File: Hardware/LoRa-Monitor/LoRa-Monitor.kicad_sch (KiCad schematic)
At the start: 0 parts

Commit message: Deleted lck files
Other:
- sheet Energy Meter Interface Module ports: added 485_A, 485_B, EN_485, PULSE_IN1+, PULSE_IN1-, PULSE_IN1_3V3, PULSE_IN2+, PULSE_IN2-, PULSE_IN2_3V3, PULSE_IN3+, PULSE_IN3-, PULSE_IN3_3V3, RXD_485, TXD_485; removed none
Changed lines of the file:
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@@
 	(paper "A4")
 	(sheet
-		(at 59.69 109.22)
+		(at 69.215 40.64)
 		(size 35.56 16.51)
 		(exclude_from_sim no)
@@
 		)
 		(property "Sheetname" "MCU"
-			(at 59.69 108.5084 0)
+			(at 69.215 39.9284 0)
 			(show_name no)
 			(do_not_autoplace no)
@@
 		)
 		(property "Sheetfile" "MCU.kicad_sch"
-			(at 59.69 126.3146 0)
+			(at 69.215 57.7346 0)
 			(show_name no)
 			(do_not_autoplace no)
@@
 	)
 	(sheet
-		(at 137.16 104.775)
+		(at 31.75 20.955)
 		(size 57.785 17.145)
 		(exclude_from_sim no)
@@
 		)
 		(property "Sheetname" "Power supply"
-			(at 137.16 104.0634 0)
+			(at 31.75 20.2434 0)
 			(show_name no)
 			(do_not_autoplace no)
@@
 		)
 		(property "Sheetfile" "PowerSupply.kicad_sch"
-			(at 137.16 122.5046 0)
+			(at 31.75 38.6846 0)
 			(show_name no)
 			(do_not_autoplace no)
@@
 			)
 		)
+		(pin "PULSE_IN2+" input
+			(at 48.26 69.85 90)
+			(effects
+				(font
+					(size 1.27 1.27)
+				)
+				(justify right)
+			)
+		)
+		(pin "PULSE_IN2-" input
+			(at 49.8793 69.85 90)
+			(effects
+				(font
+					(size 1.27 1.27)
+				)
+				(justify right)
+			)
+		)
+		(pin "PULSE_IN3+" input
+			(at 51.4986 69.85 90)
+			(effects
+				(font
+					(size 1.27 1.27)
+				)
+				(justify right)
+			)
+		)
+		(pin "PULSE_IN3-" input
+			(at 53.1179 69.85 90)
+			(effects
+				(font
+					(size 1.27 1.27)
+				)
+				(justify right)
+			)
+		)
+		(pin "RXD_485" output
+			(at 54.7372 69.85 90)
+			(effects
+				(font
+					(size 1.27 1.27)
+				)
+				(justify right)
+			)
+		)
+		(pin "EN_485" input
+			(at 56.3565 69.85 90)
+			(effects
+				(font
+					(size 1.27 1.27)
+				)
+				(justify right)
+			)
+		)
+		(pin "PULSE_IN1_3V3" output
+			(at 57.9758 69.85 90)
+			(effects
+				(font
+					(size 1.27 1.27)
+				)
+				(justify right)
+			)
+		)
+		(pin "PULSE_IN3_3V3" output
+			(at 59.5951 69.85 90)
+			(effects
+				(font
+					(size 1.27 1.27)
+				)
+				(justify right)
+			)
+		)
+		(pin "PULSE_IN2_3V3" output
+			(at 61.2144 69.85 90)
+			(effects
+				(font
+					(size 1.27 1.27)
+				)
+				(justify right)
+			)
+		)
+		(pin "TXD_485" input
+			(at 62.8337 69.85 90)
+			(effects
+				(font
+					(size 1.27 1.27)
+				)
+				(justify right)
+			)
+		)
+		(pin "485_A" bidirectional
+			(at 64.453 69.85 90)
+			(effects
+				(font
+					(size 1.27 1.27)
+				)
+				(justify right)
+			)
+		)
+		(pin "485_B" bidirectional
+			(at 80.01 85.09 0)
+			(effects
+				(font
+					(size 1.27 1.27)
+				)
+				(justify right)
+			)
+		)
+		(pin "PULSE_IN1+" input
+			(at 48.26 77.5578 180)
+			(effects
+				(font
+					(size 1.27 1.27)
+				)
+				(justify left)
+			)
+		)
+		(pin "PULSE_IN1-" input
+			(at 61.7736 69.85 90)
+			(effects
+				(font
+					(size 1.27 1.27)
+				)
+				(justify right)
+			)
+		)

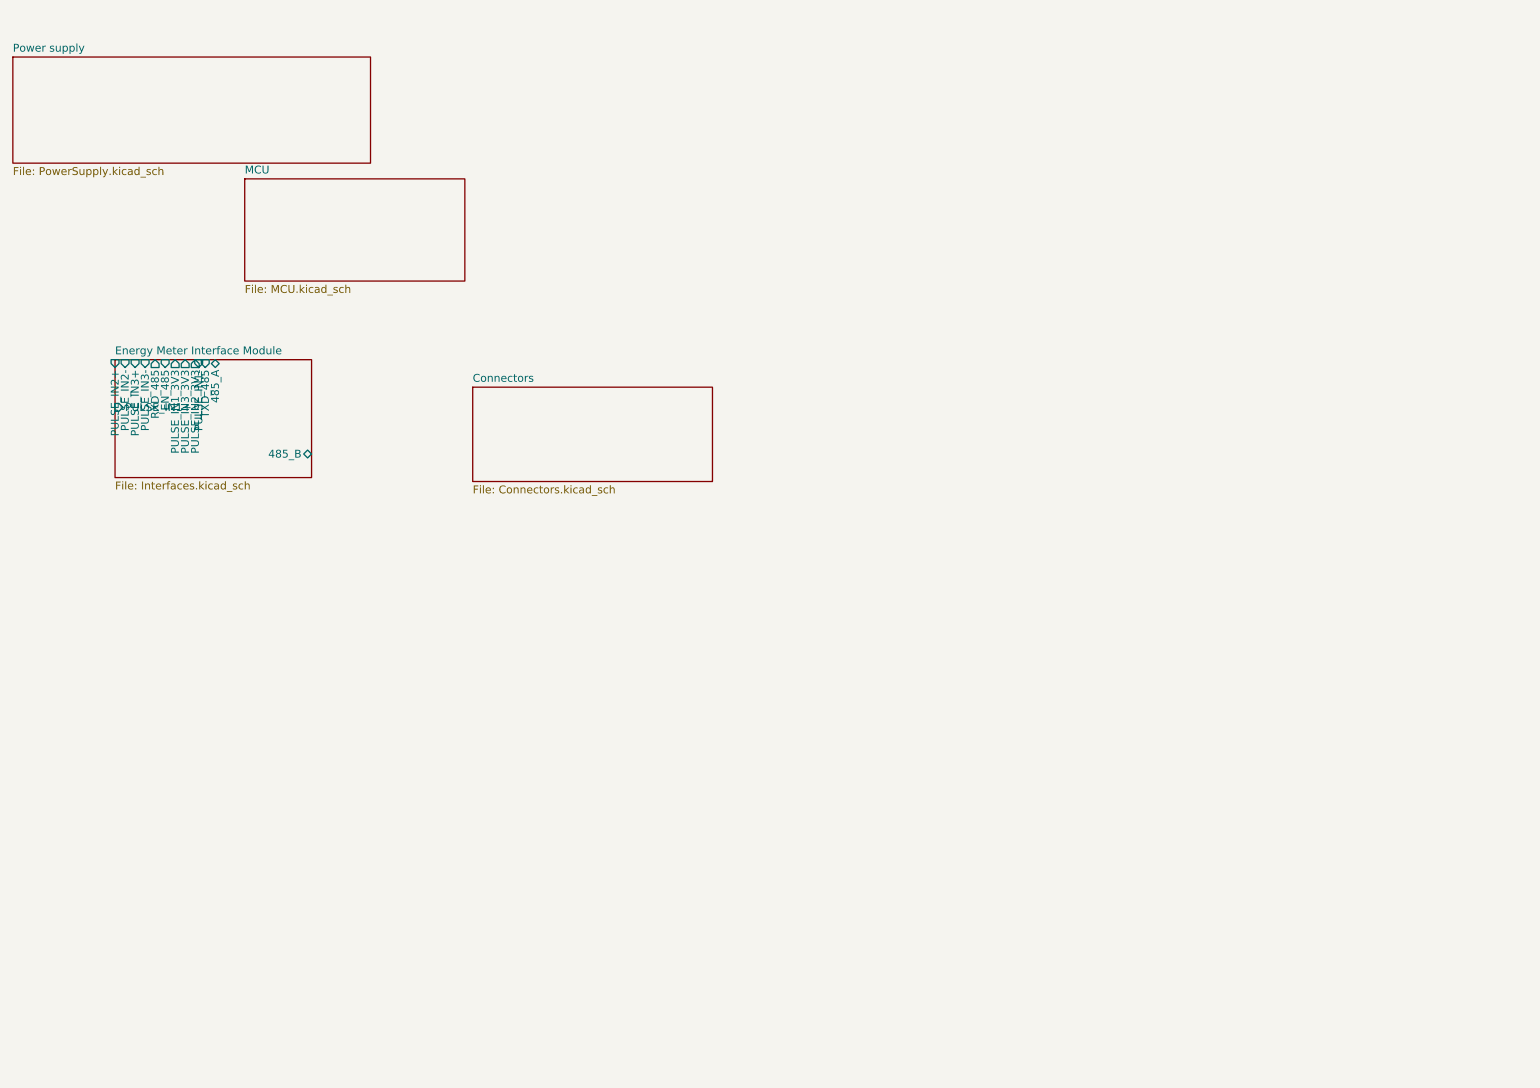
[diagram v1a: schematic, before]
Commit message: Finished PSU module, started Energy meter
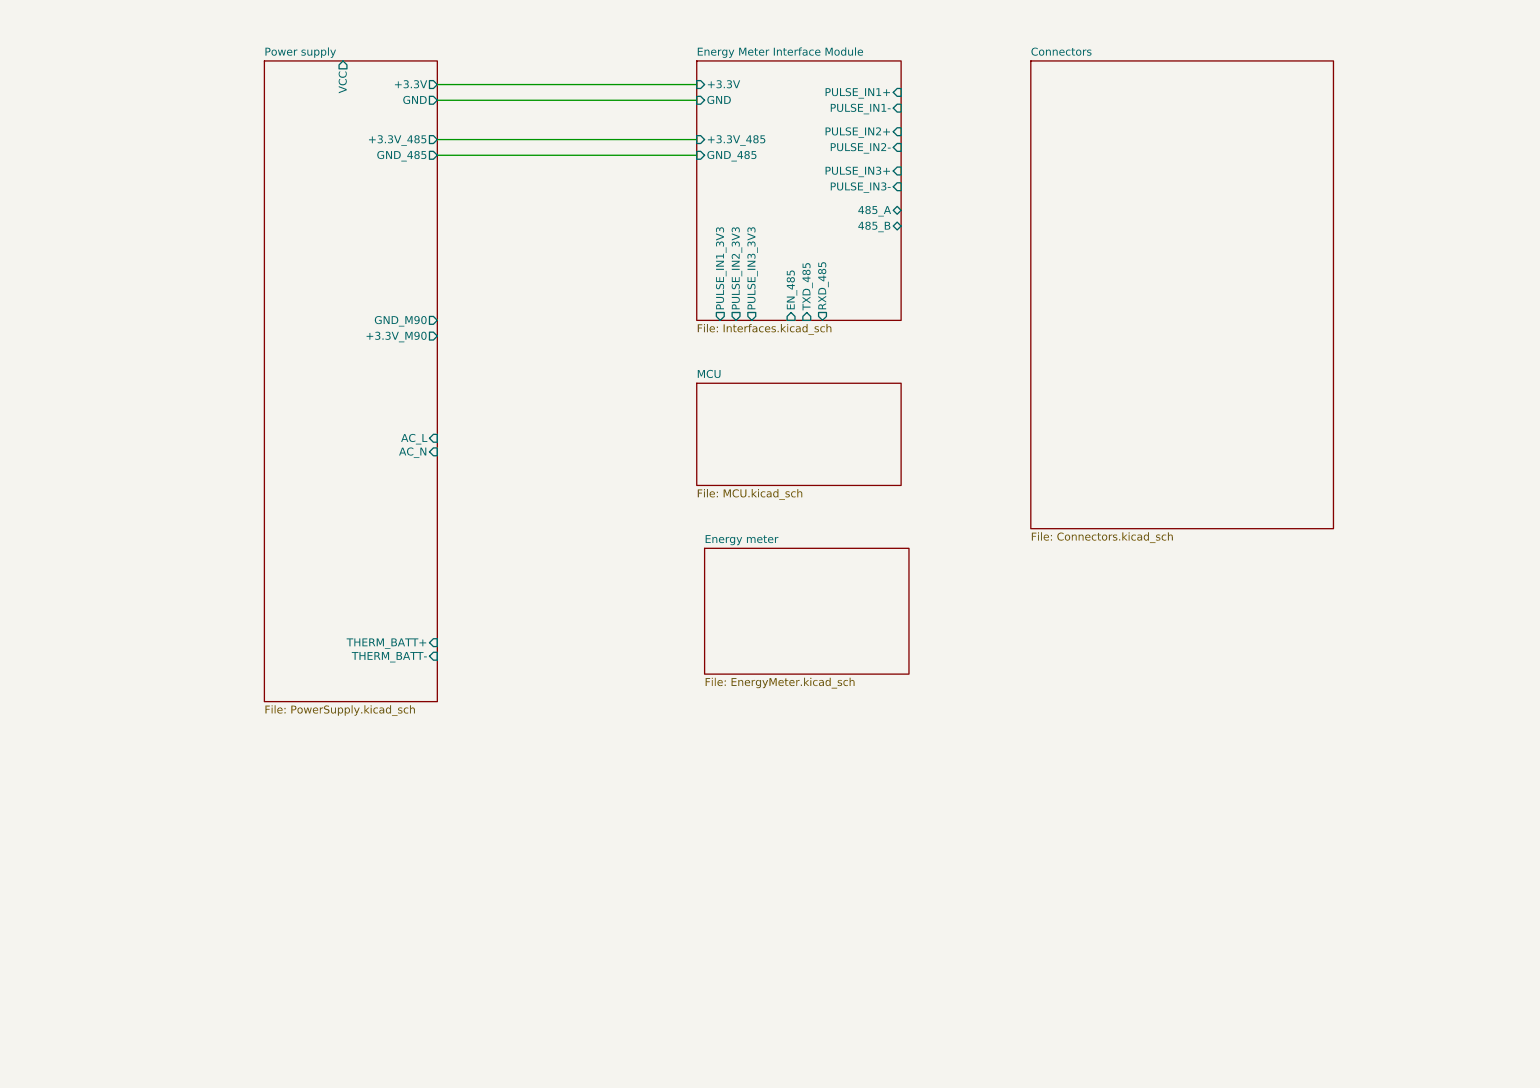
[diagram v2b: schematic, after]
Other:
- added sheet Energy meter (EnergyMeter.kicad_sch)
- sheet Energy Meter Interface Module ports: added +3.3V, +3.3V_485, GND, GND_485; removed none
- sheet Power supply ports: added +3.3V, +3.3V_485, +3.3V_M90, AC_L, AC_N, GND, GND_485, GND_M90, THERM_BATT+, THERM_BATT-, VCC; removed none

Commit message: Finished Energy Meter Module, started LoRa Module and MCU.
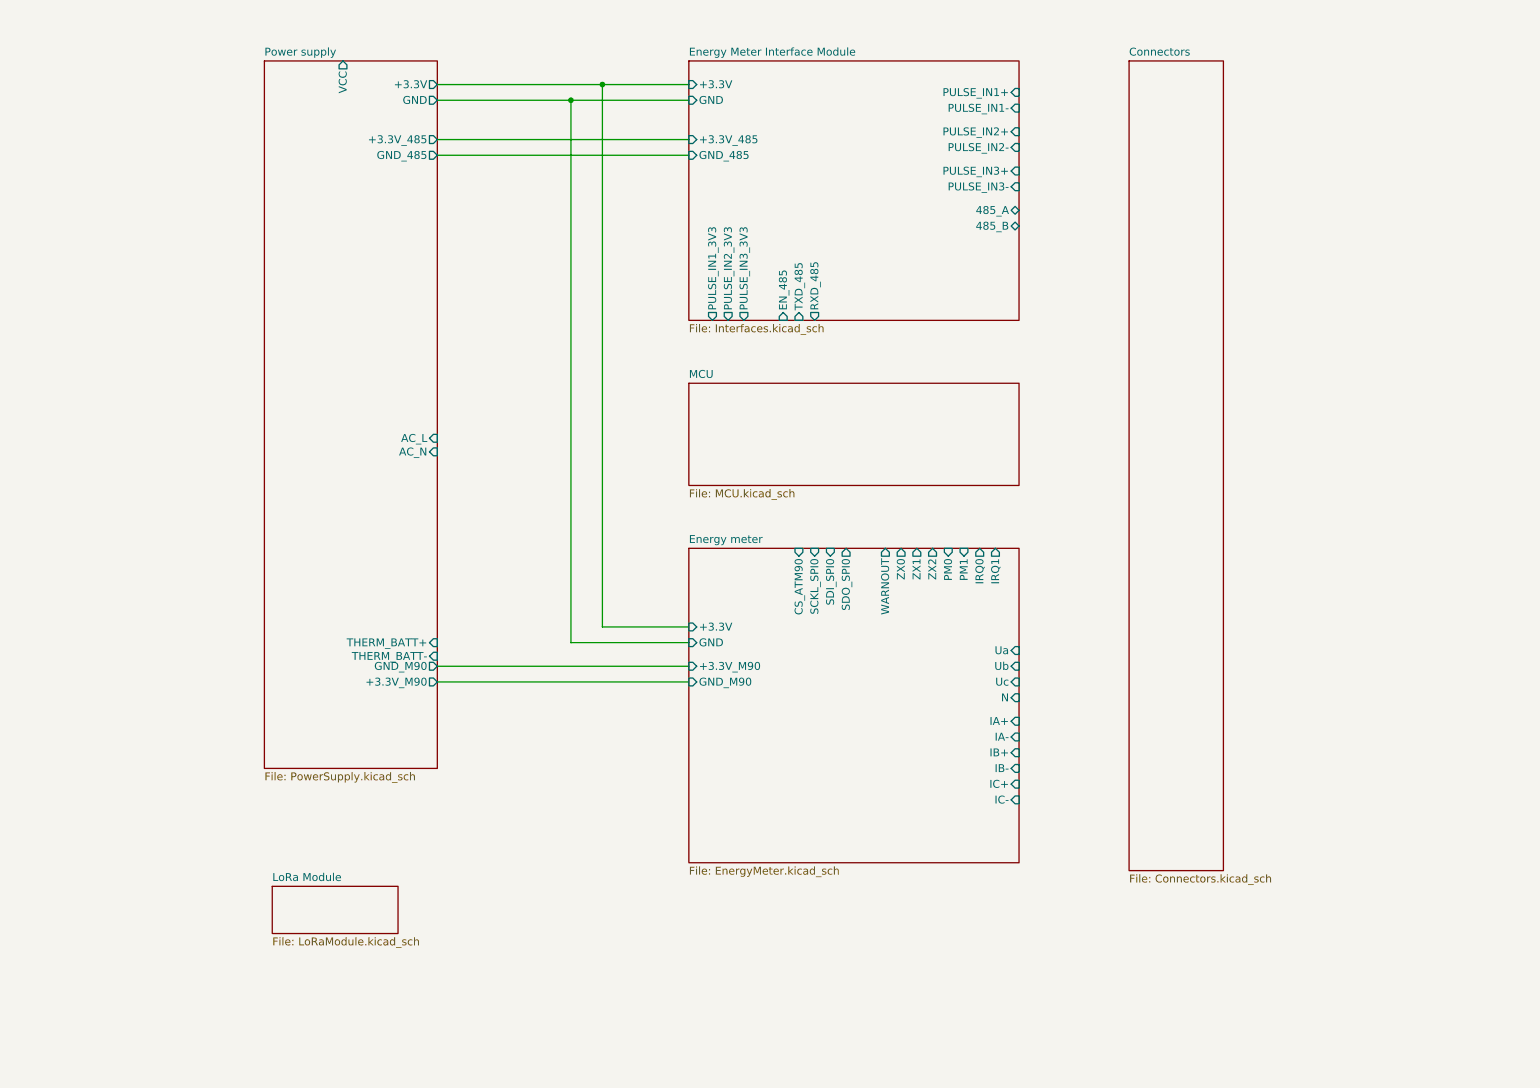
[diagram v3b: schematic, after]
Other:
- added sheet LoRa Module (LoRaModule.kicad_sch)
- sheet Energy meter ports: added +3.3V, +3.3V_M90, CS_ATM90, GND, GND_M90, IA+, IA-, IB+, IB-, IC+, IC-, IRQ0, IRQ1, N, PM0, PM1, SCKL_SPI0, SDI_SPI0, SDO_SPI0, Ua, Ub, Uc, WARNOUT, ZX0, ZX1, ZX2; removed none

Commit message: Finished MCU and Lora modules. Finished Connectors sheet
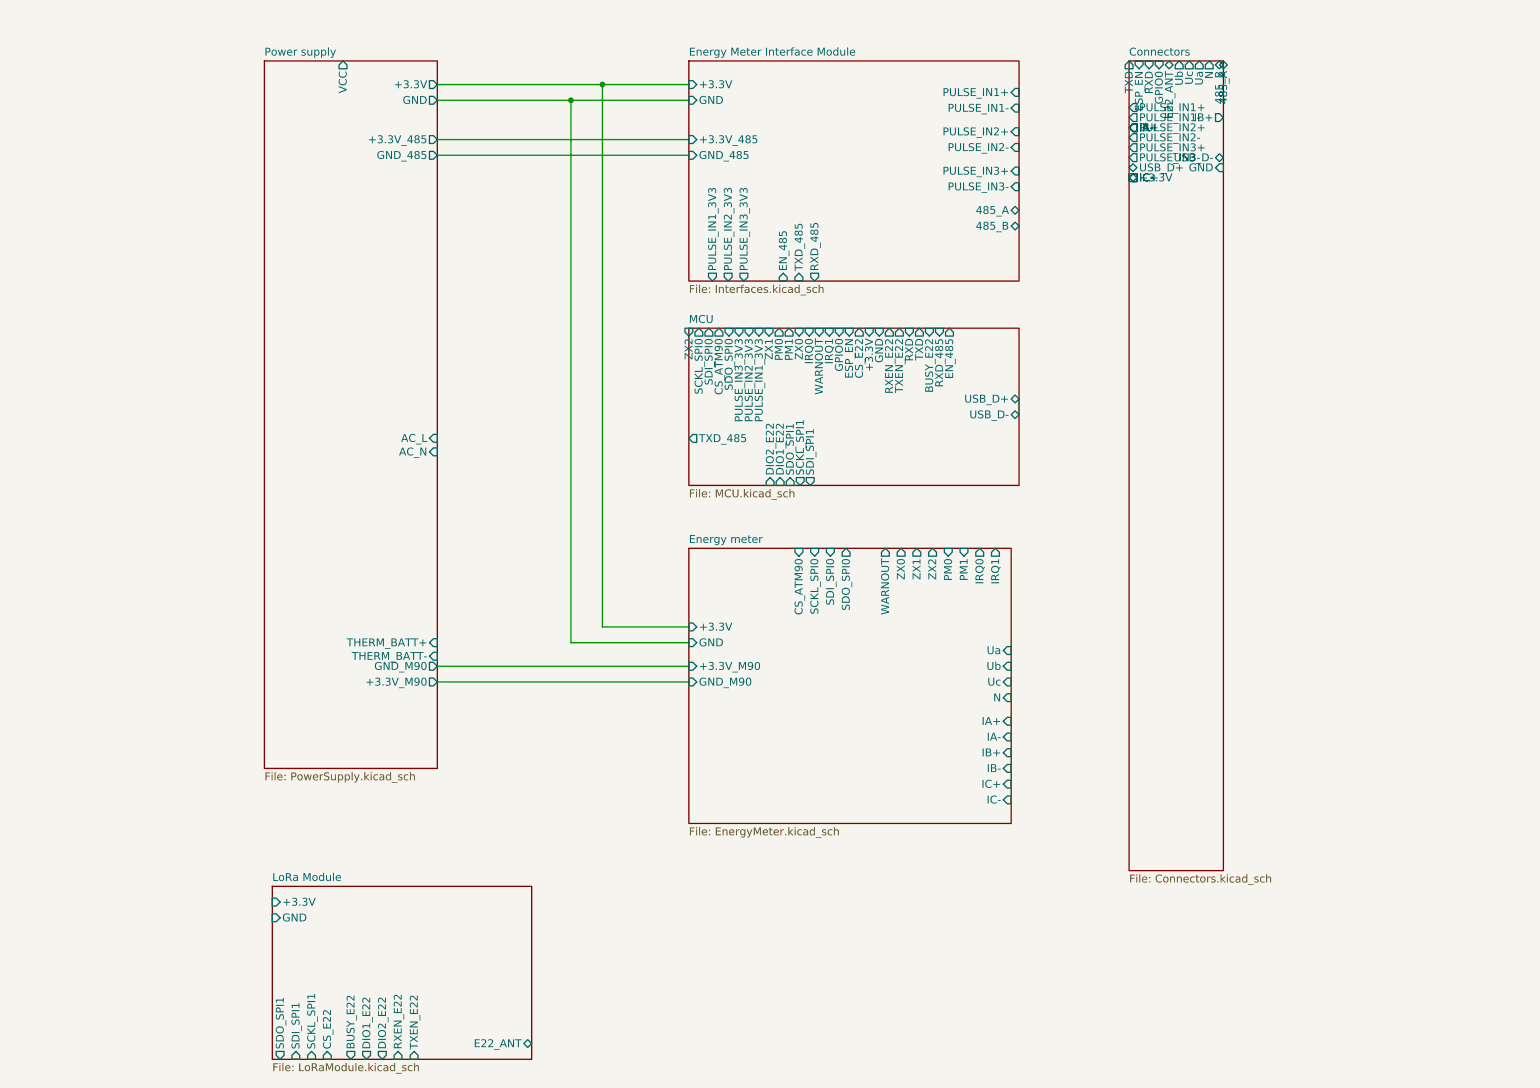
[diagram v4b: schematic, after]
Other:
- sheet Connectors ports: added +3.3V, 485_A, 485_B, E22_ANT, ESP_EN, GND, GPIO0, IA+, IA-, IB+, IB-, IC+, IC-, N, PULSE_IN1+, PULSE_IN1-, PULSE_IN2+, PULSE_IN2-, PULSE_IN3+, PULSE_IN3-, RXD, TXD, USB_D+, USB_D-, Ua, Ub, Uc; removed none
- sheet LoRa Module ports: added +3.3V, BUSY_E22, CS_E22, DIO1_E22, DIO2_E22, E22_ANT, GND, RXEN_E22, SCKL_SPI1, SDI_SPI1, SDO_SPI1, TXEN_E22; removed none
- sheet MCU ports: added +3.3V, BUSY_E22, CS_ATM90, CS_E22, DIO1_E22, DIO2_E22, EN_485, ESP_EN, GND, GPIO0, IRQ0, IRQ1, PM0, PM1, PULSE_IN1_3V3, PULSE_IN2_3V3, PULSE_IN3_3V3, RXD, RXD_485, RXEN_E22, SCKL_SPI0, SCKL_SPI1, SDI_SPI0, SDI_SPI1, SDO_SPI0, SDO_SPI1, TXD, TXD_485, TXEN_E22, USB_D+, USB_D-, WARNOUT, ZX0, ZX1, ZX2; removed none

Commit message: Finished schematic, started with PCB design
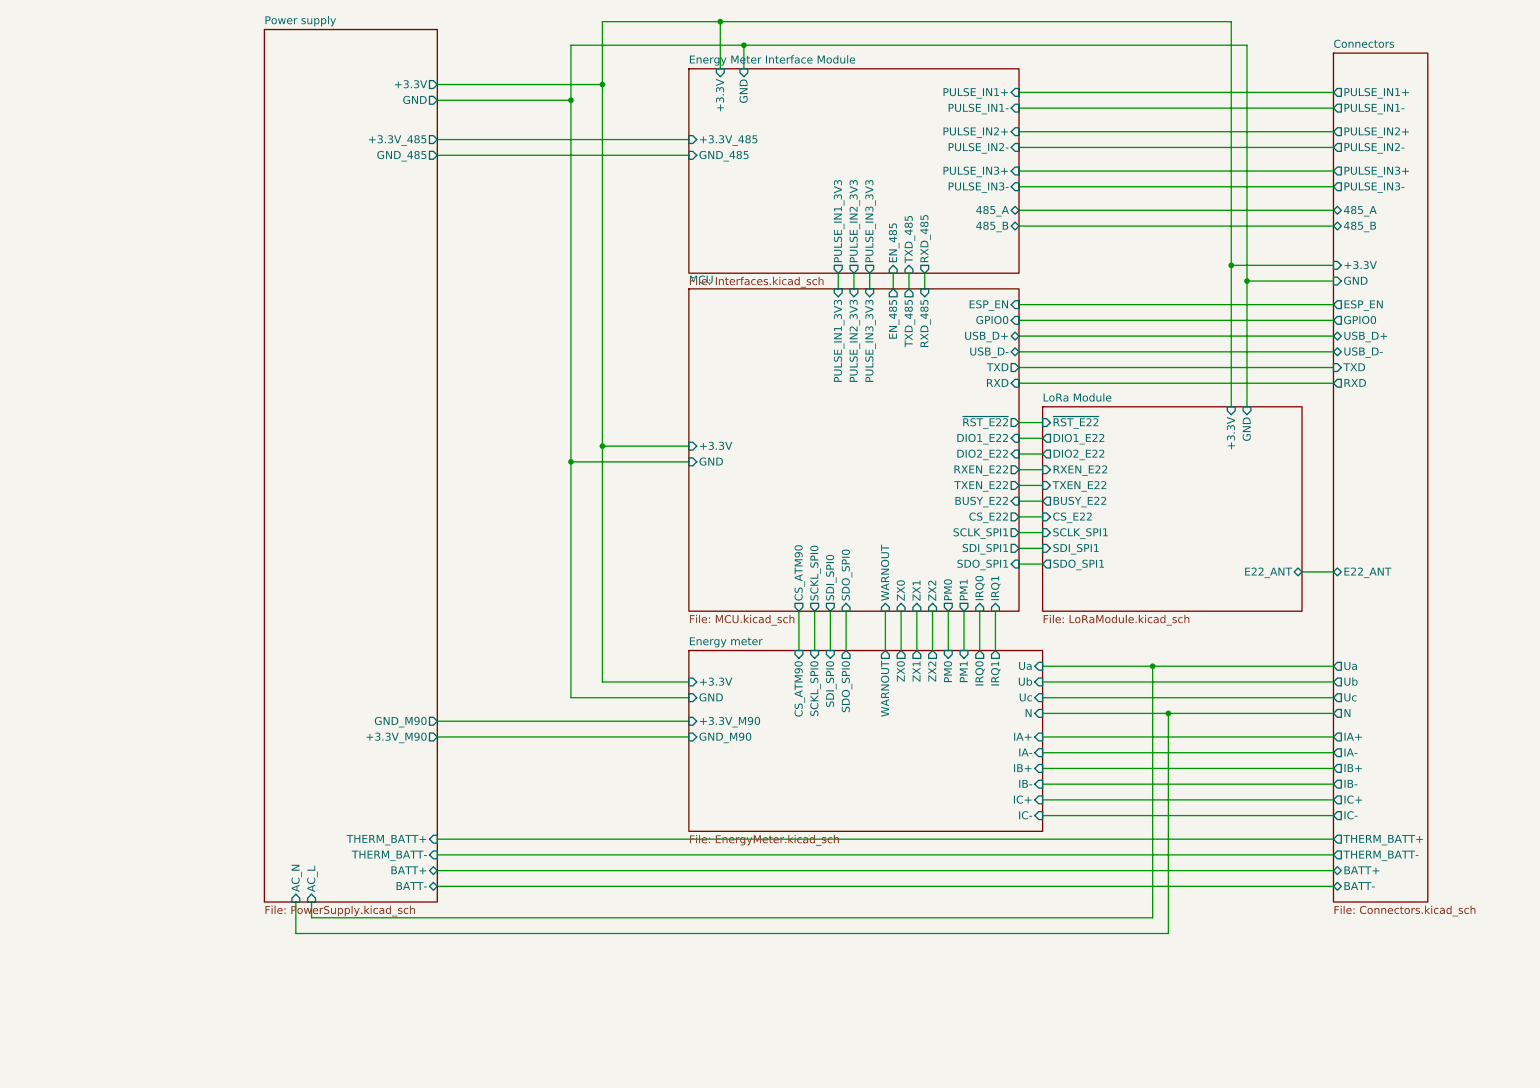
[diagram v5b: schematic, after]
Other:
- sheet Connectors ports: added BATT+, BATT-, THERM_BATT+, THERM_BATT-; removed none
- sheet LoRa Module ports: added SCLK_SPI1, ~{RST_E22}; removed SCKL_SPI1
- sheet MCU ports: added SCLK_SPI1, ~{RST_E22}; removed SCKL_SPI1
- sheet Power supply ports: added BATT+, BATT-; removed VCC
